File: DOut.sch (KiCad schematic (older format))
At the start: 18 parts

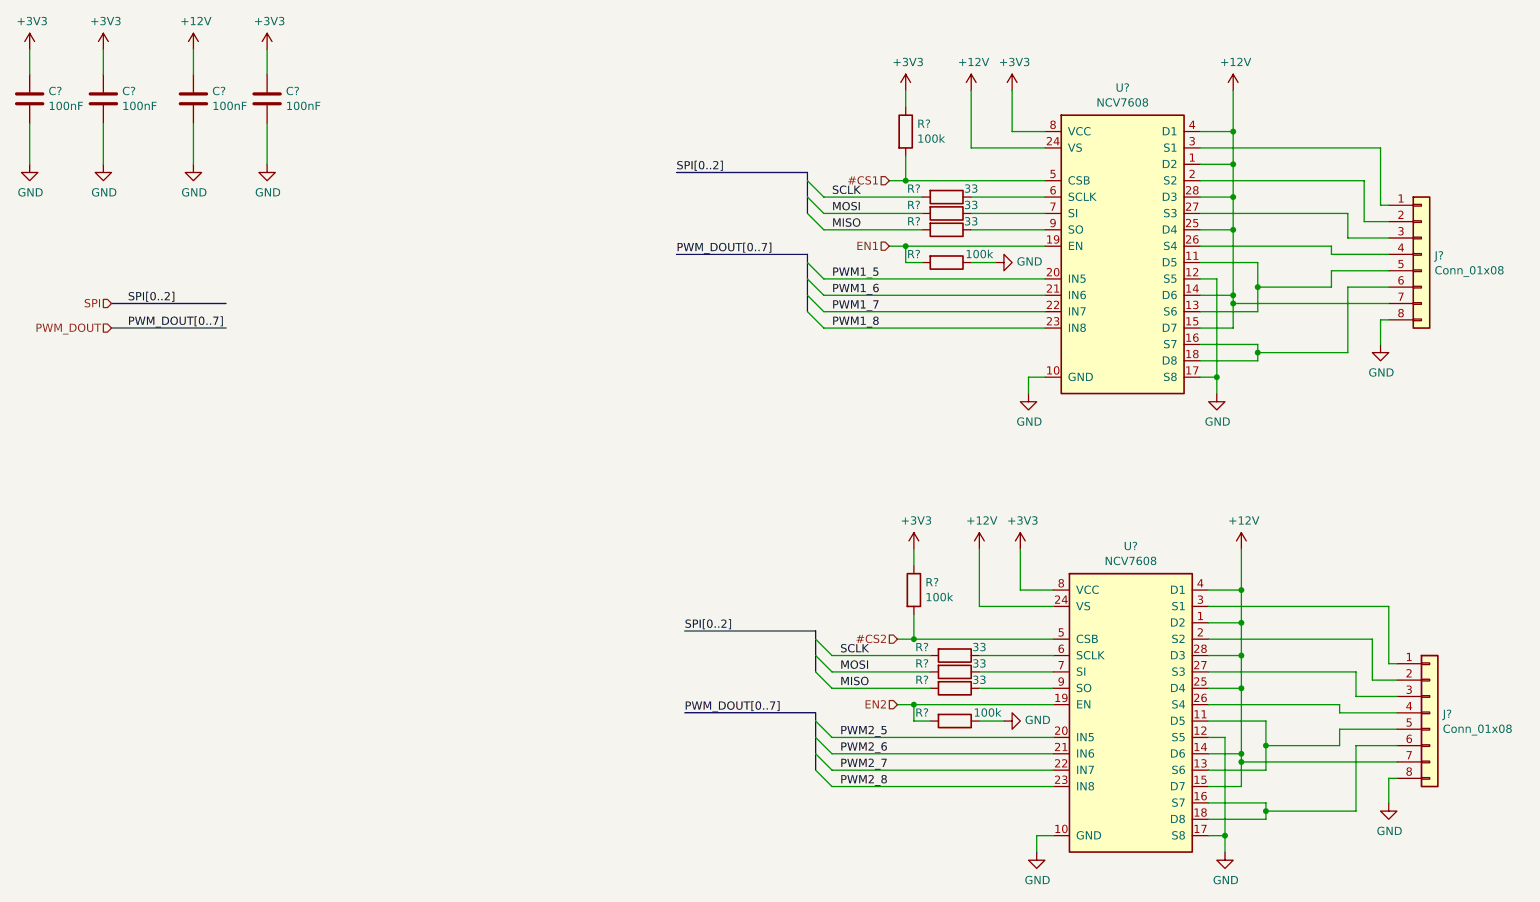
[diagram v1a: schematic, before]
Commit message: add SDcard, OneWire, Batt, analog out, digital out
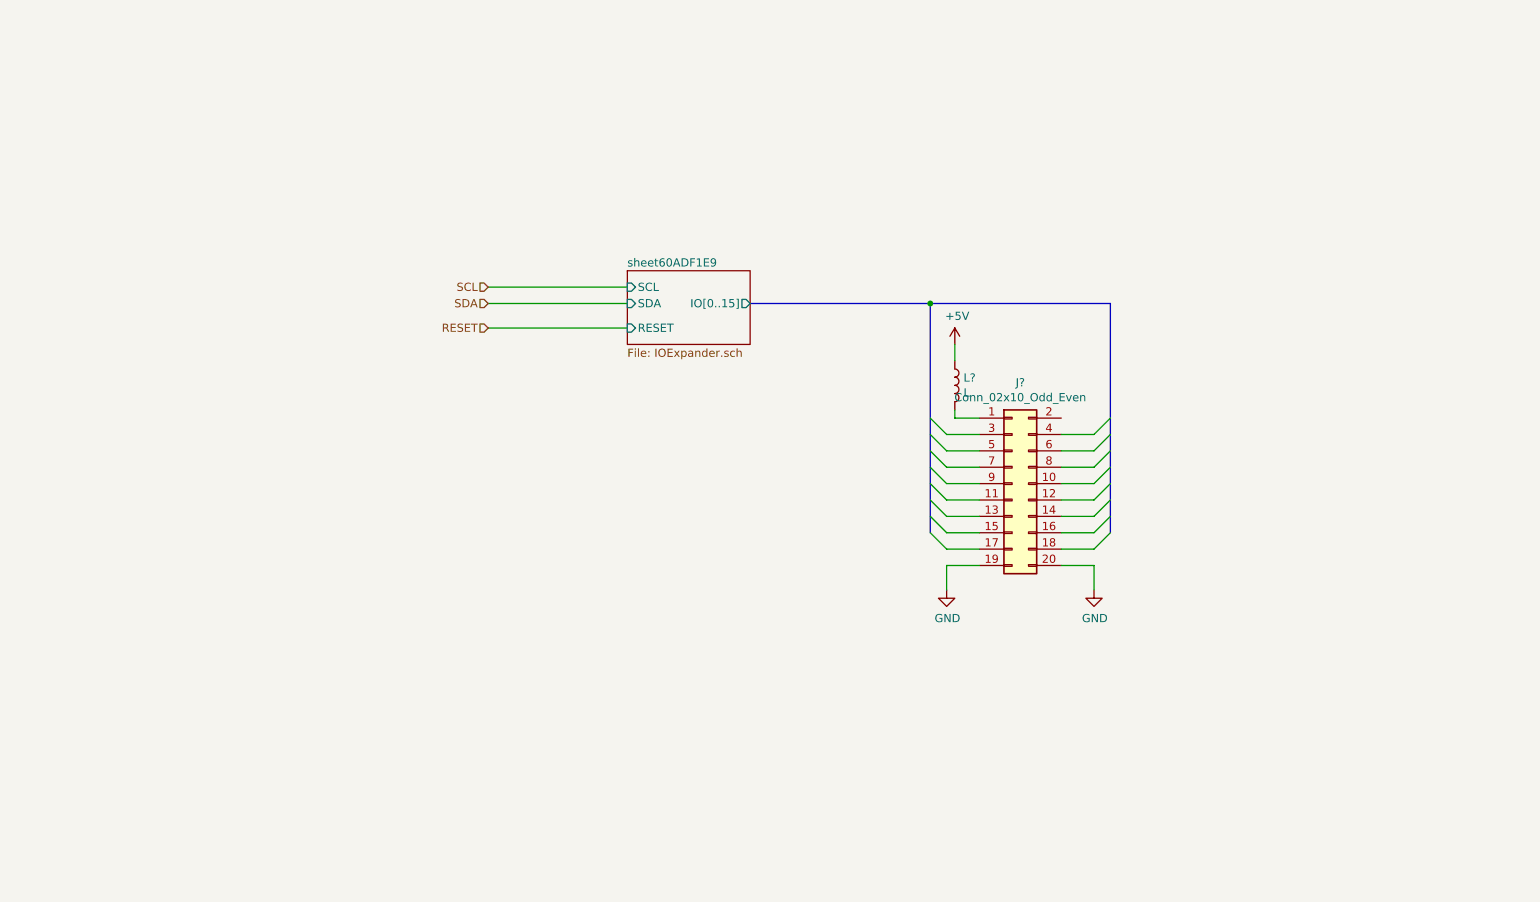
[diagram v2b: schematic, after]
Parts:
- removed C? (x4): 100nF, symbol AR2ISS:C
- removed J? (x2): Conn_01x08, symbol Connector_Generic:Conn_01x08
- removed R? (x6): 33, symbol AR2ISS:R
- removed R? (x4): 100k, symbol AR2ISS:R
- removed U? (x2): NCV7608, symbol AR2ISS:NCV7608
- added J?: Conn_02x10_Odd_Even, symbol Connector_Generic:Conn_02x10_Odd_Even
- added L?: L, symbol Device:L
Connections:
- net GND: now also J?.19 (Pin_19), J?.20 (Pin_20)
- new net: J?.1 (Pin_1), L?.2
- new net +5V: L?.1

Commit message: start placement
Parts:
- gave numbers to parts that had none: 2
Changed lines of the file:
@@
 $Descr A4 11693 8268
 encoding utf-8
-Sheet 15 19
+Sheet 15 21
 Title ""
 Date ""
@@
 	3800 2400 4650 2400
 $Comp
-L Connector_Generic:Conn_02x10_Odd_Even J?
+L Connector_Generic:Conn_02x10_Odd_Even J24
 U 1 1 60ADF6FB
 P 7000 3600
-F 0 "J?" H 7050 4217 50  0000 C CNN
+F 0 "J24" H 7050 4217 50  0000 C CNN
 F 1 "Conn_02x10_Odd_Even" H 7050 4126 50  0000 C CNN
 F 2 "" H 7000 3600 50  0001 C CNN
@@
 	6500 2500 7600 2500
 $Comp
-L power:GND #PWR?
+L power:GND #PWR0173
 U 1 1 60AE4CF1
 P 7500 4250
-F 0 "#PWR?" H 7500 4000 50  0001 C CNN
+F 0 "#PWR0173" H 7500 4000 50  0001 C CNN
 F 1 "GND" H 7505 4077 50  0000 C CNN
 F 2 "" H 7500 4250 50  0001 C CNN
@@
 $EndComp
 $Comp
-L power:GND #PWR?
+L power:GND #PWR0171
 U 1 1 60AE519E
 P 6600 4250
-F 0 "#PWR?" H 6600 4000 50  0001 C CNN
+F 0 "#PWR0171" H 6600 4000 50  0001 C CNN
 F 1 "GND" H 6605 4077 50  0000 C CNN
 F 2 "" H 6600 4250 50  0001 C CNN
@@
 	7500 4100 7500 4250
 $Comp
-L power:+5V #PWR?
+L power:+5V #PWR0172
 U 1 1 60AE77EE
 P 6650 2750
-F 0 "#PWR?" H 6650 2600 50  0001 C CNN
+F 0 "#PWR0172" H 6650 2600 50  0001 C CNN
 F 1 "+5V" H 6665 2923 50  0000 C CNN
 F 2 "" H 6650 2750 50  0001 C CNN
@@
 $EndComp
 $Comp
-L Device:L L?
+L Device:L L27
 U 1 1 60AE7C4C
 P 6650 3000
-F 0 "L?" H 6703 3046 50  0000 L CNN
+F 0 "L27" H 6703 3046 50  0000 L CNN
 F 1 "L" H 6703 2955 50  0000 L CNN
 F 2 "" H 6650 3000 50  0001 C CNN

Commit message: placement
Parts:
- J24: footprint (none) -> Connector_IDC:IDC-Header_2x10_P2.54mm_Vertical
- L27: footprint (none) -> Inductor_SMD:L_0603_1608Metric
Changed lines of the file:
@@
 $Descr A4 11693 8268
 encoding utf-8
-Sheet 15 21
+Sheet 13 22
 Title ""
 Date ""
@@
 F 0 "J24" H 7050 4217 50  0000 C CNN
 F 1 "Conn_02x10_Odd_Even" H 7050 4126 50  0000 C CNN
-F 2 "" H 7000 3600 50  0001 C CNN
+F 2 "Connector_IDC:IDC-Header_2x10_P2.54mm_Vertical" H 7000 3600 50  0001 C CNN
 F 3 "~" H 7000 3600 50  0001 C CNN
 	1    7000 3600
@@
 F 0 "L27" H 6703 3046 50  0000 L CNN
 F 1 "L" H 6703 2955 50  0000 L CNN
-F 2 "" H 6650 3000 50  0001 C CNN
+F 2 "Inductor_SMD:L_0603_1608Metric" H 6650 3000 50  0001 C CNN
 F 3 "~" H 6650 3000 50  0001 C CNN
 	1    6650 3000

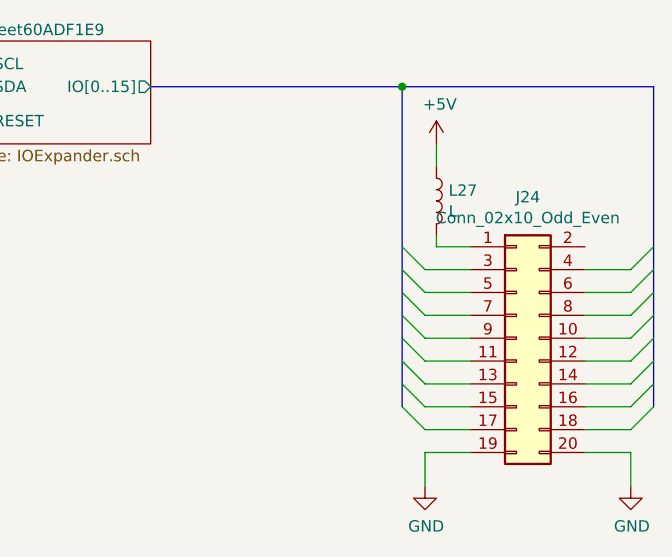
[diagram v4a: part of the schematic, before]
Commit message: add TLE5602
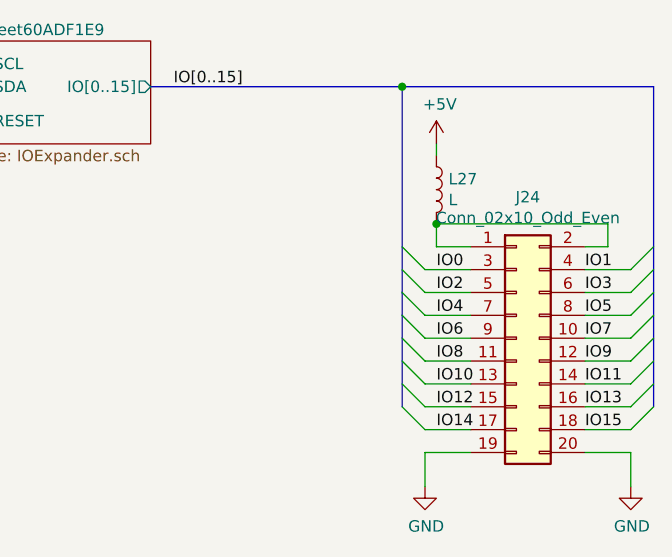
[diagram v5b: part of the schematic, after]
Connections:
- net at J24.1 (Pin_1), L27.2: now also J24.2 (Pin_2)
- net IO7: now reaches J24.10 (Pin_10)
- net IO8: now reaches J24.11 (Pin_11)
- net IO9: now reaches J24.12 (Pin_12)
- net IO10: now reaches J24.13 (Pin_13)
- net IO11: now reaches J24.14 (Pin_14)
- net IO12: now reaches J24.15 (Pin_15)
- net IO13: now reaches J24.16 (Pin_16)
- net IO14: now reaches J24.17 (Pin_17)
- net IO15: now reaches J24.18 (Pin_18)
- net IO0: now reaches J24.3 (Pin_3)
- net IO1: now reaches J24.4 (Pin_4)
- net IO2: now reaches J24.5 (Pin_5)
- net IO3: now reaches J24.6 (Pin_6)
- net IO4: now reaches J24.7 (Pin_7)
- net IO5: now reaches J24.8 (Pin_8)
- net IO6: now reaches J24.9 (Pin_9)
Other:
- moved on the sheet: L27
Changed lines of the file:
@@
 $Descr A4 11693 8268
 encoding utf-8
-Sheet 13 22
+Sheet 12 22
 Title ""
 Date ""
@@
 L Device:L L27
 U 1 1 60AE7C4C
-P 6650 3000
-F 0 "L27" H 6703 3046 50  0000 L CNN
-F 1 "L" H 6703 2955 50  0000 L CNN
-F 2 "Inductor_SMD:L_0603_1608Metric" H 6650 3000 50  0001 C CNN
-F 3 "~" H 6650 3000 50  0001 C CNN
-	1    6650 3000
+P 6650 2950
+F 0 "L27" H 6703 2996 50  0000 L CNN
+F 1 "L" H 6703 2905 50  0000 L CNN
+F 2 "Inductor_SMD:L_0603_1608Metric" H 6650 2950 50  0001 C CNN
+F 3 "~" H 6650 2950 50  0001 C CNN
+	1    6650 2950
 	1    0    0    -1
 $EndComp
@@
 	6800 3200 6650 3200
 Wire Wire Line
-	6650 3200 6650 3150
-Wire Wire Line
-	6650 2750 6650 2850
+	6650 3200 6650 3100
+Wire Wire Line
+	6650 2750 6650 2800
+Text Label 5500 2500 0    50   ~ 0
+IO[0..15]
+Wire Wire Line
+	7300 3200 7400 3200
+Wire Wire Line
+	7400 3200 7400 3100
+Wire Wire Line
+	7400 3100 6650 3100
+Connection ~ 6650 3100
+Text Label 6650 3300 0    50   ~ 0
+IO0
+Text Label 7300 3300 0    50   ~ 0
+IO1
+Text Label 6650 3400 0    50   ~ 0
+IO2
+Text Label 7300 3400 0    50   ~ 0
+IO3
+Text Label 6650 3500 0    50   ~ 0
+IO4
+Text Label 7300 3500 0    50   ~ 0
+IO5
+Text Label 6650 3600 0    50   ~ 0
+IO6
+Text Label 7300 3600 0    50   ~ 0
+IO7
+Text Label 6650 3700 0    50   ~ 0
+IO8
+Text Label 7300 3700 0    50   ~ 0
+IO9
+Text Label 6650 3800 0    50   ~ 0
+IO10
+Text Label 7300 3800 0    50   ~ 0
+IO11
+Text Label 6650 3900 0    50   ~ 0
+IO12
+Text Label 7300 3900 0    50   ~ 0
+IO13
+Text Label 6650 4000 0    50   ~ 0
+IO14
+Text Label 7300 4000 0    50   ~ 0
+IO15
 Wire Bus Line
 	6500 2500 6500 3900

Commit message: ready for jlc
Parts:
- added R121: 4.7k, Resistor_SMD:R_0603_1608Metric, symbol AR2ISS:R
- added R122, R123: NB, Resistor_SMD:R_0603_1608Metric, symbol AR2ISS:R
- added R124: 0R, Resistor_SMD:R_0603_1608Metric, symbol AR2ISS:R
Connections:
- net +5V: now also R121.1, R123.1
- net GND: now also R122.2, R124.2
- new net sheet60ADF1E9/A0: R123.2, R124.1
- new net sheet60ADF1E9/A1: R121.2, R122.1
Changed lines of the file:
@@
 $Descr A4 11693 8268
 encoding utf-8
-Sheet 12 22
+Sheet 11 22
 Title ""
 Date ""
@@
 $EndDescr
 $Sheet
-S 4650 2300 750  450
+S 4650 2300 750  1200
 U 60ADF1EF
 F0 "sheet60ADF1E9" 50
@@
 F4 "RESET" I L 4650 2650 50
 F5 "IO[0..15]" O R 5400 2500 50
+F6 "A0" I L 4650 3300 50
+F7 "A1" I L 4650 3200 50
+F8 "A2" I L 4650 3100 50
 $EndSheet
 Text HLabel 3800 2400 0    50   Input ~ 0
@@
 Text Label 7300 4000 0    50   ~ 0
 IO15
+$Comp
+L AR2ISS:R R?
+U 1 1 60A7591A
+P 3050 3550
+AR Path="/60679D69/60A7591A" Ref="R?"  Part="1"
+AR Path="/607267A8/60A7591A" Ref="R?"  Part="1"
+AR Path="/60A2B663/60A7591A" Ref="R?"  Part="1"
+AR Path="/60A2BC9C/60A7591A" Ref="R?"  Part="1"
+AR Path="/60ADDFFD/60A7591A" Ref="R?"  Part="1"
+AR Path="/60ADEB0F/60ADF1EF/60A7591A" Ref="R?"  Part="1"
+AR Path="/60A7591A" Ref="R?"  Part="1"
+AR Path="/60ADEB0F/60A7591A" Ref="R124"  Part="1"
+F 0 "R124" H 3120 3596 50  0000 L CNN
+F 1 "0R" H 3120 3505 50  0000 L CNN
+F 2 "Resistor_SMD:R_0603_1608Metric" V 2980 3550 50  0001 C CNN
+F 3 "~" H 3050 3550 50  0001 C CNN
+	1    3050 3550
+	1    0    0    -1
+$EndComp
+$Comp
+L power:GND #PWR?
+U 1 1 60A75920
+P 3050 3750
+AR Path="/607267A8/60A75920" Ref="#PWR?"  Part="1"
+AR Path="/60679D69/60A75920" Ref="#PWR?"  Part="1"
+AR Path="/60A2B663/60A75920" Ref="#PWR?"  Part="1"
+AR Path="/60A2BC9C/60A75920" Ref="#PWR?"  Part="1"
+AR Path="/60ADDFFD/60A75920" Ref="#PWR?"  Part="1"
+AR Path="/60ADEB0F/60ADF1EF/60A75920" Ref="#PWR?"  Part="1"
+AR Path="/60A75920" Ref="#PWR?"  Part="1"
+AR Path="/60ADEB0F/60A75920" Ref="#PWR0176"  Part="1"
+F 0 "#PWR0176" H 3050 3500 50  0001 C CNN
+F 1 "GND" H 3055 3577 50  0000 C CNN
+F 2 "" H 3050 3750 50  0001 C CNN
+F 3 "" H 3050 3750 50  0001 C CNN
+	1    3050 3750
+	1    0    0    -1
+$EndComp
+Wire Wire Line
+	3050 3700 3050 3750
+$Comp
+L AR2ISS:R R?
+U 1 1 60A75927
+P 2800 3550
+AR Path="/60679D69/60A75927" Ref="R?"  Part="1"
+AR Path="/607267A8/60A75927" Ref="R?"  Part="1"
+AR Path="/60A2B663/60A75927" Ref="R?"  Part="1"
+AR Path="/60A2BC9C/60A75927" Ref="R?"  Part="1"
+AR Path="/60ADDFFD/60A75927" Ref="R?"  Part="1"
+AR Path="/60ADEB0F/60ADF1EF/60A75927" Ref="R?"  Part="1"
+AR Path="/60A75927" Ref="R?"  Part="1"
+AR Path="/60ADEB0F/60A75927" Ref="R122"  Part="1"
+F 0 "R122" H 2870 3596 50  0000 L CNN
+F 1 "NB" H 2870 3505 50  0000 L CNN
+F 2 "Resistor_SMD:R_0603_1608Metric" V 2730 3550 50  0001 C CNN
+F 3 "~" H 2800 3550 50  0001 C CNN
+	1    2800 3550
+	1    0    0    -1
+$EndComp
+$Comp
+L power:GND #PWR?
+U 1 1 60A7592D
+P 2800 3750
+AR Path="/607267A8/60A7592D" Ref="#PWR?"  Part="1"
+AR Path="/60679D69/60A7592D" Ref="#PWR?"  Part="1"
+AR Path="/60A2B663/60A7592D" Ref="#PWR?"  Part="1"
+AR Path="/60A2BC9C/60A7592D" Ref="#PWR?"  Part="1"
+AR Path="/60ADDFFD/60A7592D" Ref="#PWR?"  Part="1"
+AR Path="/60ADEB0F/60ADF1EF/60A7592D" Ref="#PWR?"  Part="1"
+AR Path="/60A7592D" Ref="#PWR?"  Part="1"
+AR Path="/60ADEB0F/60A7592D" Ref="#PWR0177"  Part="1"
+F 0 "#PWR0177" H 2800 3500 50  0001 C CNN
+F 1 "GND" H 2805 3577 50  0000 C CNN
+F 2 "" H 2800 3750 50  0001 C CNN
+F 3 "" H 2800 3750 50  0001 C CNN
+	1    2800 3750
+	1    0    0    -1
+$EndComp
+Wire Wire Line
+	2800 3700 2800 3750
+$Comp
+L power:+5V #PWR?
+U 1 1 60A75934
+P 3050 2200
+AR Path="/607267A8/60A75934" Ref="#PWR?"  Part="1"
+AR Path="/60679D69/60A75934" Ref="#PWR?"  Part="1"
+AR Path="/60A2B663/60A75934" Ref="#PWR?"  Part="1"
+AR Path="/60A2BC9C/60A75934" Ref="#PWR?"  Part="1"
+AR Path="/60ADDFFD/60A75934" Ref="#PWR?"  Part="1"
+AR Path="/60ADEB0F/60ADF1EF/60A75934" Ref="#PWR?"  Part="1"
+AR Path="/60A75934" Ref="#PWR?"  Part="1"
+AR Path="/60ADEB0F/60A75934" Ref="#PWR0178"  Part="1"
+F 0 "#PWR0178" H 3050 2050 50  0001 C CNN
+F 1 "+5V" H 3065 2373 50  0000 C CNN
+F 2 "" H 3050 2200 50  0001 C CNN
+F 3 "" H 3050 2200 50  0001 C CNN
+	1    3050 2200
+	1    0    0    -1
+$EndComp
+$Comp
+L power:+5V #PWR?
+U 1 1 60A7593A
+P 2800 2200
+AR Path="/607267A8/60A7593A" Ref="#PWR?"  Part="1"
+AR Path="/60679D69/60A7593A" Ref="#PWR?"  Part="1"
+AR Path="/60A2B663/60A7593A" Ref="#PWR?"  Part="1"
+AR Path="/60A2BC9C/60A7593A" Ref="#PWR?"  Part="1"
+AR Path="/60ADDFFD/60A7593A" Ref="#PWR?"  Part="1"
+AR Path="/60ADEB0F/60ADF1EF/60A7593A" Ref="#PWR?"  Part="1"
+AR Path="/60A7593A" Ref="#PWR?"  Part="1"
+AR Path="/60ADEB0F/60A7593A" Ref="#PWR0213"  Part="1"
+F 0 "#PWR0213" H 2800 2050 50  0001 C CNN
+F 1 "+5V" H 2815 2373 50  0000 C CNN
+F 2 "" H 2800 2200 50  0001 C CNN
+F 3 "" H 2800 2200 50  0001 C CNN
+	1    2800 2200
+	1    0    0    -1
+$EndComp
+Wire Wire Line
+	2800 3200 2800 3400
+Connection ~ 2800 3200
+Wire Wire Line
+	3050 3400 3050 3300
+Connection ~ 3050 3300
+Wire Wire Line
+	2800 3200 4650 3200
+Wire Wire Line
+	3050 3300 4650 3300
+$Comp
+L AR2ISS:R R?
+U 1 1 60A75947
+P 2800 2450
+AR Path="/60679D69/60A75947" Ref="R?"  Part="1"
+AR Path="/607267A8/60A75947" Ref="R?"  Part="1"
+AR Path="/60A2B663/60A75947" Ref="R?"  Part="1"
+AR Path="/60A2BC9C/60A75947" Ref="R?"  Part="1"
+AR Path="/60ADDFFD/60A75947" Ref="R?"  Part="1"
+AR Path="/60ADEB0F/60ADF1EF/60A75947" Ref="R?"  Part="1"
+AR Path="/60A75947" Ref="R?"  Part="1"
+AR Path="/60ADEB0F/60A75947" Ref="R121"  Part="1"
+F 0 "R121" H 2870 2496 50  0000 L CNN
+F 1 "4.7k" H 2870 2405 50  0000 L CNN
+F 2 "Resistor_SMD:R_0603_1608Metric" V 2730 2450 50  0001 C CNN
+F 3 "~" H 2800 2450 50  0001 C CNN
+	1    2800 2450
+	1    0    0    -1
+$EndComp
+$Comp
+L AR2ISS:R R?
+U 1 1 60A7594D
+P 3050 2450
+AR Path="/60679D69/60A7594D" Ref="R?"  Part="1"
+AR Path="/607267A8/60A7594D" Ref="R?"  Part="1"
+AR Path="/60A2B663/60A7594D" Ref="R?"  Part="1"
+AR Path="/60A2BC9C/60A7594D" Ref="R?"  Part="1"
+AR Path="/60ADDFFD/60A7594D" Ref="R?"  Part="1"
+AR Path="/60ADEB0F/60ADF1EF/60A7594D" Ref="R?"  Part="1"
+AR Path="/60A7594D" Ref="R?"  Part="1"
+AR Path="/60ADEB0F/60A7594D" Ref="R123"  Part="1"
+F 0 "R123" H 3120 2496 50  0000 L CNN
+F 1 "NB" H 3120 2405 50  0000 L CNN
+F 2 "Resistor_SMD:R_0603_1608Metric" V 2980 2450 50  0001 C CNN
+F 3 "~" H 3050 2450 50  0001 C CNN
+	1    3050 2450
+	1    0    0    -1
+$EndComp
+Wire Wire Line
+	3050 2600 3050 3300
+Wire Wire Line
+	2800 2600 2800 3200
+Wire Wire Line
+	2800 2300 2800 2200
+Wire Wire Line
+	3050 2200 3050 2300
+$Comp
+L power:GND #PWR?
+U 1 1 60A7B8D9
+P 4500 3100
+AR Path="/607267A8/60A7B8D9" Ref="#PWR?"  Part="1"
+AR Path="/60679D69/60A7B8D9" Ref="#PWR?"  Part="1"
+AR Path="/60A2B663/60A7B8D9" Ref="#PWR?"  Part="1"
+AR Path="/60A2BC9C/60A7B8D9" Ref="#PWR?"  Part="1"
+AR Path="/60ADDFFD/60A7B8D9" Ref="#PWR?"  Part="1"
+AR Path="/60ADEB0F/60ADF1EF/60A7B8D9" Ref="#PWR?"  Part="1"
+AR Path="/60A7B8D9" Ref="#PWR?"  Part="1"
+AR Path="/60ADEB0F/60A7B8D9" Ref="#PWR0216"  Part="1"
+F 0 "#PWR0216" H 4500 2850 50  0001 C CNN
+F 1 "GND" H 4505 2927 50  0000 C CNN
+F 2 "" H 4500 3100 50  0001 C CNN
+F 3 "" H 4500 3100 50  0001 C CNN
+	1    4500 3100
+	0    1    1    0
+$EndComp
+Wire Wire Line
+	4500 3100 4650 3100
 Wire Bus Line
 	6500 2500 6500 3900
